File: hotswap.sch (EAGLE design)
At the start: 13 parts

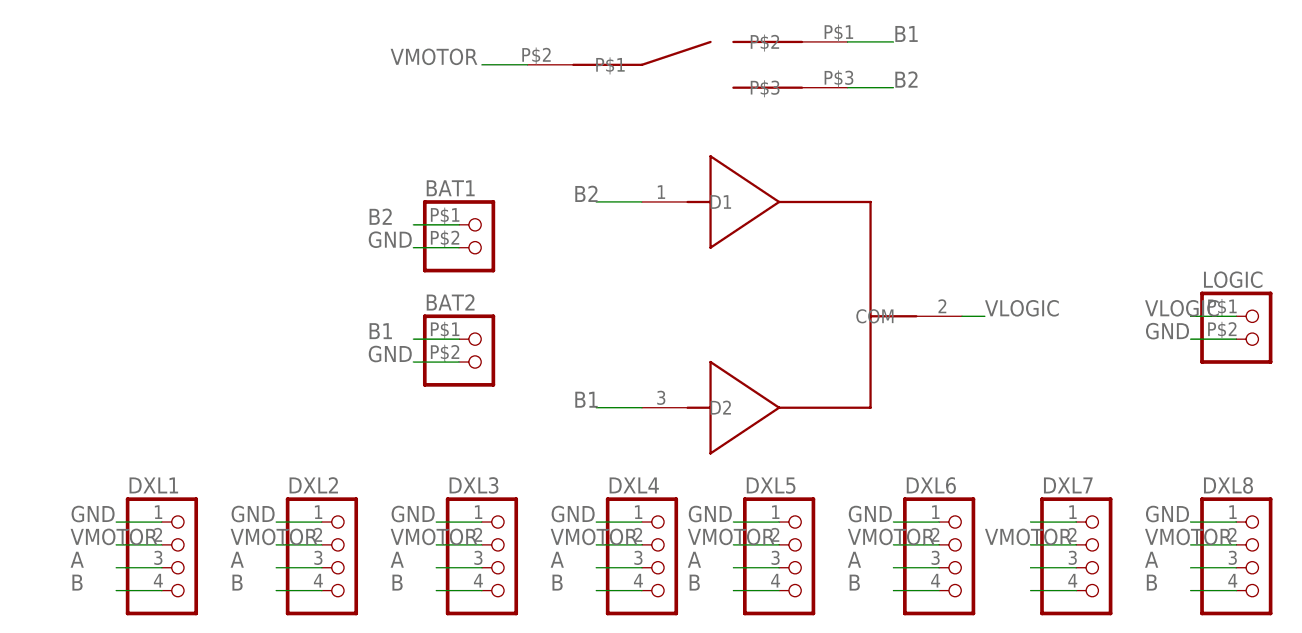
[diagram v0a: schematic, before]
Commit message: Fixing FARNELL attributes and writing BOM
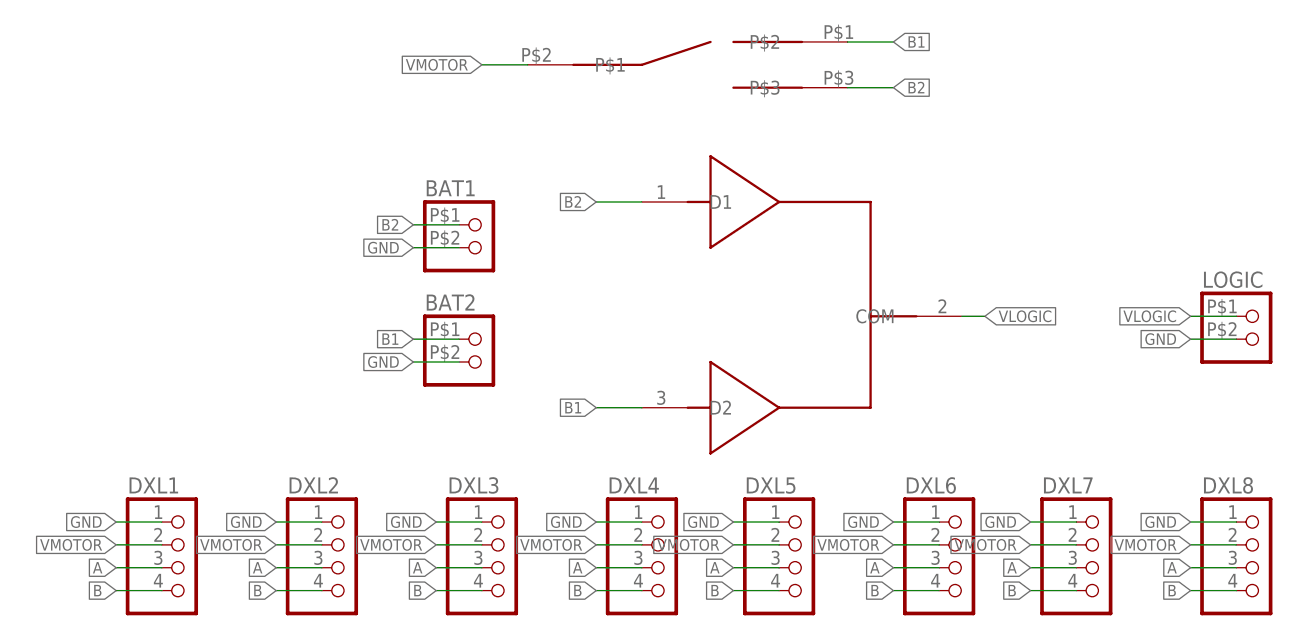
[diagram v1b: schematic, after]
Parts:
- DXL1, DXL2, DXL3, DXL4, DXL5, DXL6, DXL7, DXL8: FARNELL (none) -> 9979620 OR 1104204
- U$1: FARNELL (none) -> 1431049
- U$2: FARNELL (none) -> 150551
